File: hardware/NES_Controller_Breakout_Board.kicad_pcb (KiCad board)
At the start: 2 copper layers, 50 x 50 mm, 6 parts, among them J2 Conn_01x05_Socket

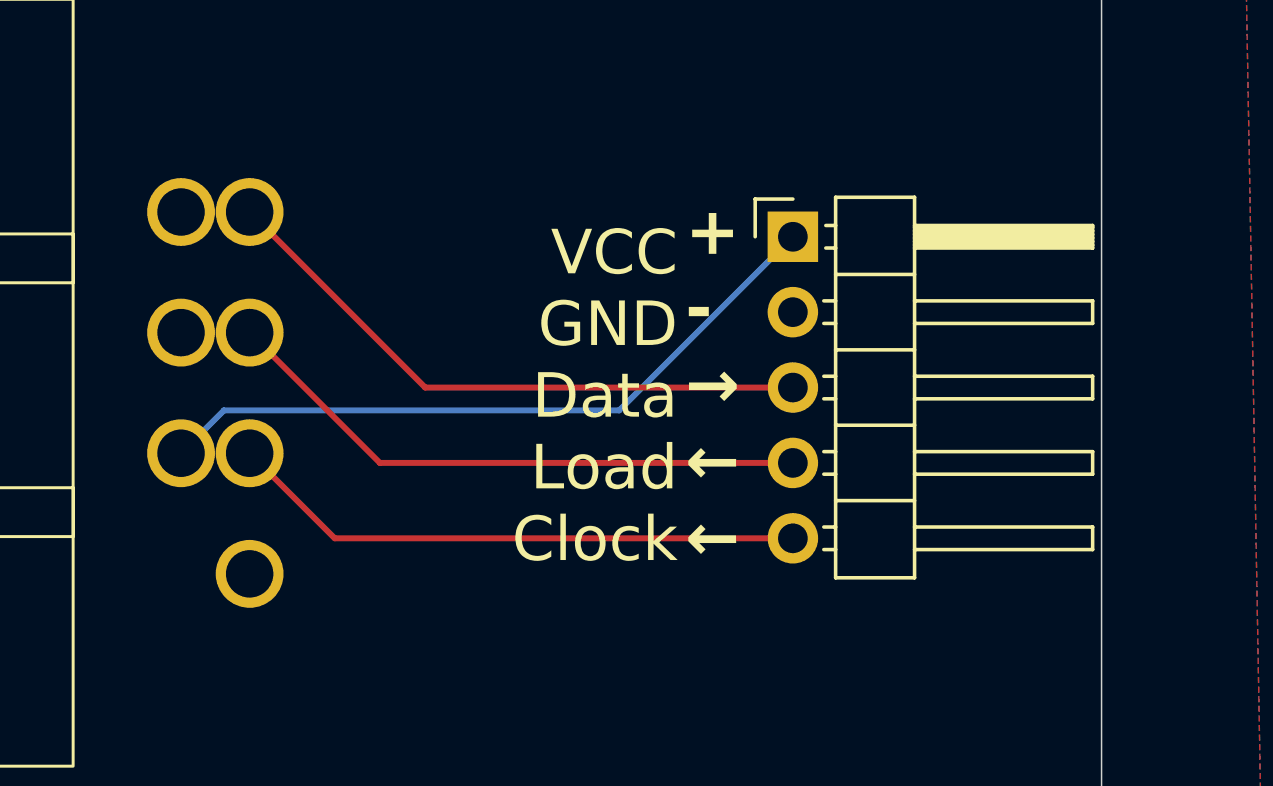
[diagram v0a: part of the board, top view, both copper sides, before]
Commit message: Scaled text up
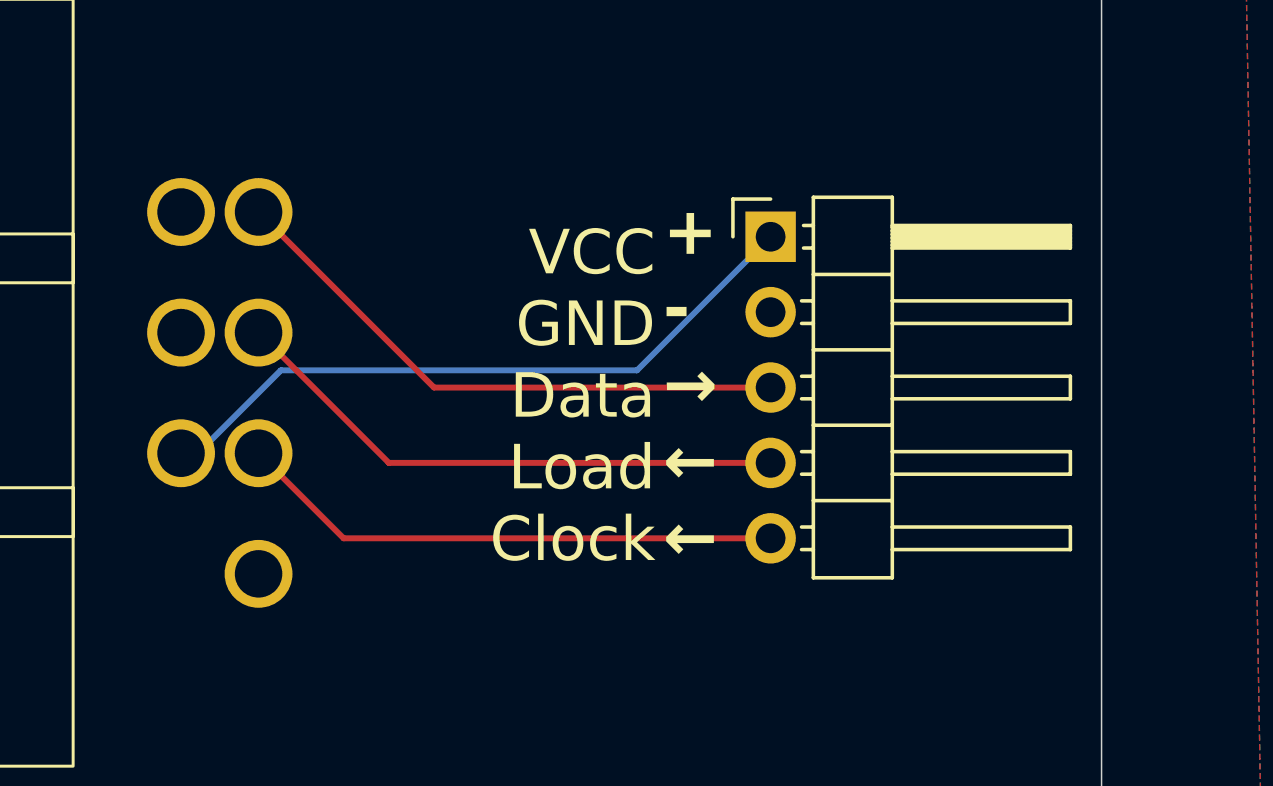
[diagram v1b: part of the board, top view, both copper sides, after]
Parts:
- moved J2 0.75 mm to (170.8, 115.0)
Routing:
- net Load: track 20.1 -> 19.1 mm
- net Data: track 20.8 -> 19.7 mm
- net Clock: track 19.5 -> 18.4 mm
- net VCC: track 23.6 -> 22.9 mm
